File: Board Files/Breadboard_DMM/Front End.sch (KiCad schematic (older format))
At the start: 20 parts, among them J401 V+, J402 I+, J403 COM, K401 EC2-5NU, K402 EC2-5NU, Q401 NTZD3154N, U401 LMV358

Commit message: Updated probe connector arrangement
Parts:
- removed J403: COM, Connector_PinHeader_2.54mm:PinHeader_1x02_P2.54mm_Vertical, symbol Connector_Generic:Conn_01x02
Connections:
- net labels added: COM, I+, V+
- wire segments 110 -> 106
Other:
- note removed: "Front End"
- moved on the sheet: J401, J402, K401A, K402A, K402B, Q401A, Q401B, R405, R406, R407, R408, R409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

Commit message: Semi-finished component placement
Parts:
- C301: renamed from C401; footprint Resistor_SMD:R_0603_1608Metric_Pad1.05x0.95mm_HandSolder -> Capacitor_SMD:C_0603_1608Metric_Pad1.08x0.95mm_HandSolder
- D301: renamed from D401; symbol Device:D_ALT -> Device:D_Filled
- D302: renamed from D402; symbol Device:D_ALT -> Device:D_Filled
- J301: renamed from J401; footprint Connector_PinHeader_2.54mm:PinHeader_1x02_P2.54mm_Vertical -> Connector_PinSocket_2.54mm:PinSocket_1x02_P2.54mm_Vertical; Digi-Key Link https://www.digikey.com/en/products/detail/samtec-inc/SSW-101-01-T-S/1112304 ; https://www.digikey.com/en/products/detail/adam-tech/PH1-01-UA/9830231 -> https://www.digikey.com/en/products/detail/samtec-inc/SSW-102-01-T-S/1112303; Digi-Key PN SAM1213-01-ND; 2057-PH1-01-UA-ND -> SAM1213-02-ND
- J302: renamed from J402; footprint Connector_PinHeader_2.54mm:PinHeader_1x02_P2.54mm_Vertical -> Connector_PinSocket_2.54mm:PinSocket_1x02_P2.54mm_Vertical; Digi-Key Link https://www.digikey.com/en/products/detail/samtec-inc/SSW-101-01-T-S/1112304 ; https://www.digikey.com/en/products/detail/adam-tech/PH1-01-UA/9830231 -> https://www.digikey.com/en/products/detail/samtec-inc/SSW-102-01-T-S/1112303; Digi-Key PN SAM1213-01-ND; 2057-PH1-01-UA-ND -> SAM1213-02-ND
- K301: renamed from K402; MPN (none) -> EC2-5NU
- K302: renamed from K401; MPN (none) -> EC2-5NU
- Q301: renamed from Q401; value NTZD3154N -> BSD840N; footprint Package_TO_SOT_SMD:SOT-563 -> Package_TO_SOT_SMD:SOT-363_SC-70-6_Handsoldering; Digi-Key Link https://www.digikey.com/en/products/detail/on-semiconductor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 -> https://www.digikey.com/en/products/detail/infineon-technol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; Digi-Key PN NTZD3154NT1GOSCT-ND -> BSD840NH6327XTSA1CT-ND; MPN (none) -> BSD840NH6327XTSA1
- R303: renamed from R404; Digi-Key Link https://www.digikey.com/en/products/detail/yageo/RT0805BRD0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 -> https://www.digikey.com/en/products/detail/susumu/RR1220P-8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; Digi-Key PN YAG1978CT-ND -> RR12P820KDCT-ND; Tolerance 0.1% -> 0.5%
- renumbered R401 to R301, R402 to R302, R403 to R304, R405 to R305, R406 to R306, R407 to R307, R408 to R308, R409 to R309, R410 to R310, U401 to U301
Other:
- moved on the sheet: K301B, K301C, K302B, K302C, R301, R302, R303, R304

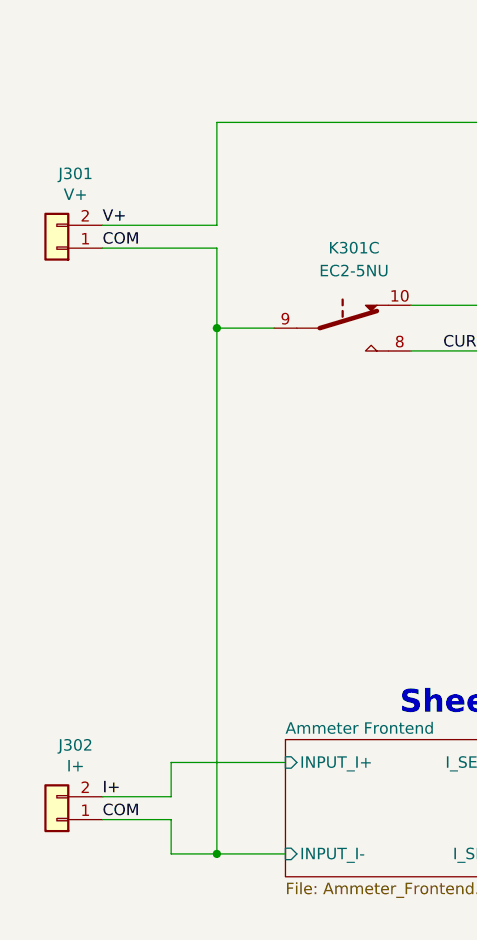
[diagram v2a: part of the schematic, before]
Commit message: Added silkscreen graphics and BOM
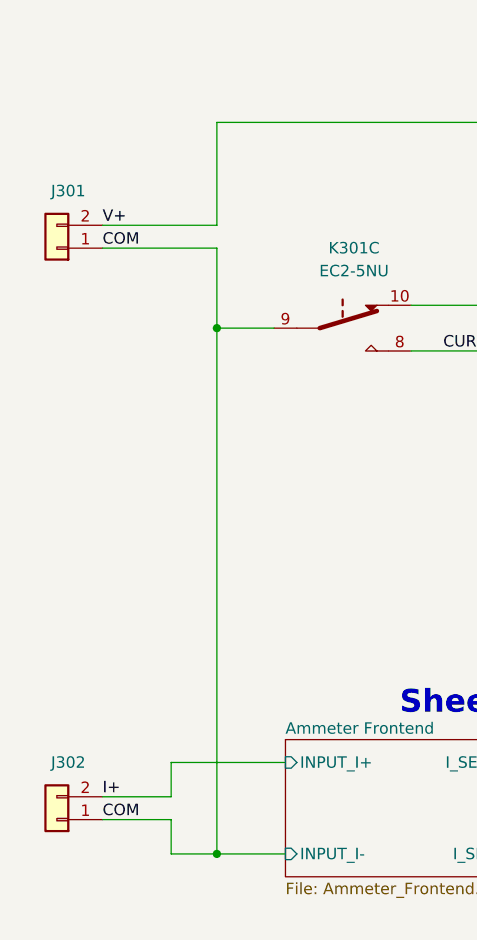
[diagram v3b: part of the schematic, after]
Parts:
- J301: value V+ -> Conn_01x02
- J302: value I+ -> Conn_01x02
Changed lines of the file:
@@
 U 1 1 5F91B0FE
 P 1450 5200
-F 0 "J302" H 1368 4875 50  0000 C CNN
-F 1 "I+" H 1368 4966 50  0000 C CNN
+F 0 "J302" H 1400 4950 50  0000 C CNN
+F 1 "Conn_01x02" H 1350 4950 50  0001 C CNN
 F 2 "Connector_PinSocket_2.54mm:PinSocket_1x02_P2.54mm_Vertical" H 1450 5200 50  0001 C CNN
 F 3 "~" H 1450 5200 50  0001 C CNN
@@
 U 1 1 5F915A3B
 P 1450 2700
-F 0 "J301" H 1368 2375 50  0000 C CNN
-F 1 "V+" H 1368 2466 50  0000 C CNN
+F 0 "J301" H 1400 2450 50  0000 C CNN
+F 1 "Conn_01x02" H 1350 2450 50  0001 C CNN
 F 2 "Connector_PinSocket_2.54mm:PinSocket_1x02_P2.54mm_Vertical" H 1450 2700 50  0001 C CNN
 F 3 "~" H 1450 2700 50  0001 C CNN
